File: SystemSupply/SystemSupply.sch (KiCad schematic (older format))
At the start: 14 parts

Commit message: Added DC/DC converters symbols to Library. Added DC/DC converters, purging valve parts and bus connectors to the SystemSupply schematic.
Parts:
- removed NT?: Net-Tie_2, symbol Device:Net-Tie_2
- added C?: 10n, symbol Device:C
- added C?: 470u, symbol Device:CP
- added C?: 180u, symbol Device:CP
- added D? (x2): D_ALT, symbol Device:D_ALT
- added D?: D_TVS_ALT, symbol Device:D_TVS_ALT
- added J? (x2): 4P4C, symbol Connector:4P4C
- added J? (x3): Screw_Terminal_01x02, symbol Connector:Screw_Terminal_01x02
- added JP?: Jumper_NO_Small, symbol Device:Jumper_NO_Small
- added L? (x2): 3u, symbol Device:L
- added Q?: Q_NMOS_GSD, symbol Device:Q_NMOS_GSD
- added R?: 1Meg, symbol Device:R
- added R?: 2k, symbol Device:R
- added R?: 10k, symbol Device:R
- added R?: 120, symbol Device:R
- added SW? (x2): SW_SPST, symbol Switch:SW_SPST
- added SW?: SW_Push, symbol Switch:SW_Push
- added U?: LTV-817S, Package_DIP:SMDIP-4_W9.53mm, symbol Isolator:LTV-817S
- added U?: DCDC_LM2596, symbol Library:DCDC_LM2596
- added U?: AXA01B18-L, symbol Library:AXA01B18-L
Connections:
- net labels added: +12V, IN+, IN-, OUT+, OUT-
- wire segments 20 -> 72
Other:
- note added: "Dodatkowe złącze magistrali"
- note added: "Filtr wejściowy"
- note added: "Filtr wyjściowy"
- note added: "Podły chińczyk"
- note added: "Przemysłowy pewniak"
- note added: "Przycisk zaworu wylotowego"
- note added: "Terminacja magistrali"
- note added: "Włącznik zasilania magistrali"
- note added: "Zasilanie sterownika ogniwa"
- note added: "Złącze elektrozaworu wylotowego"
- note added: "Złącze magistrali"
- note added: "Złącze sygnału elektrozaworu\nwylotowego"
- moved on the sheet: C?, D?, F?, J?, K?, Q?, R?, U?

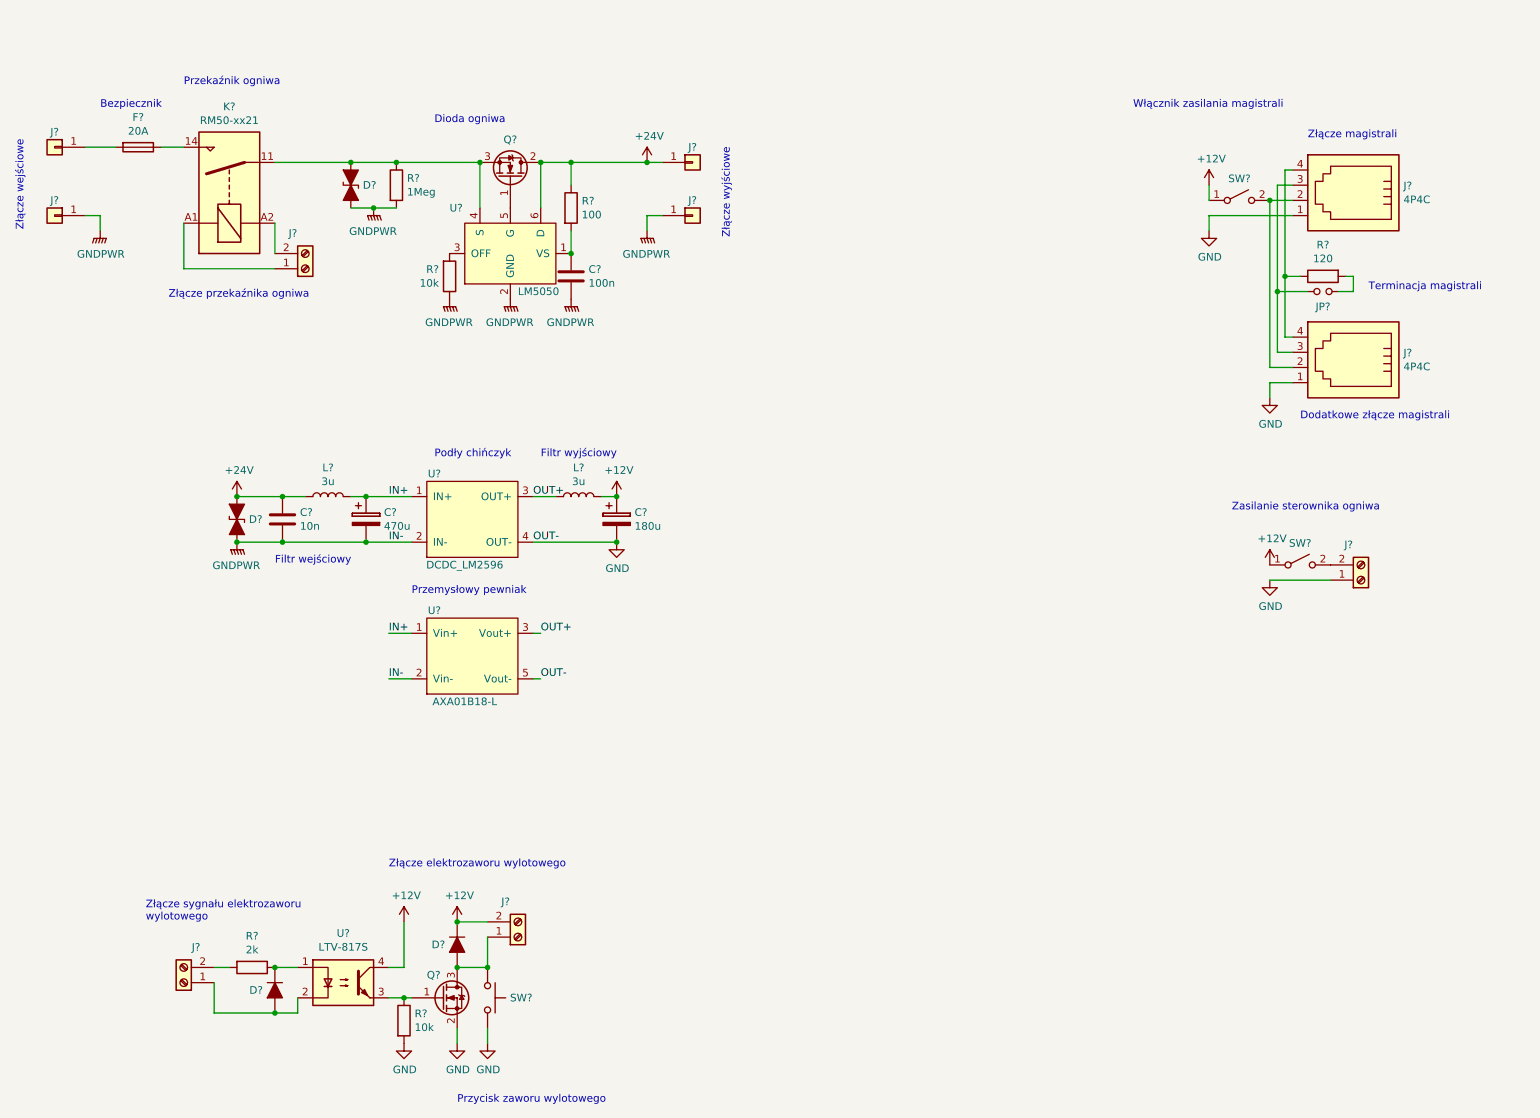
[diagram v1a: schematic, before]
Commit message: Added ground jumper.
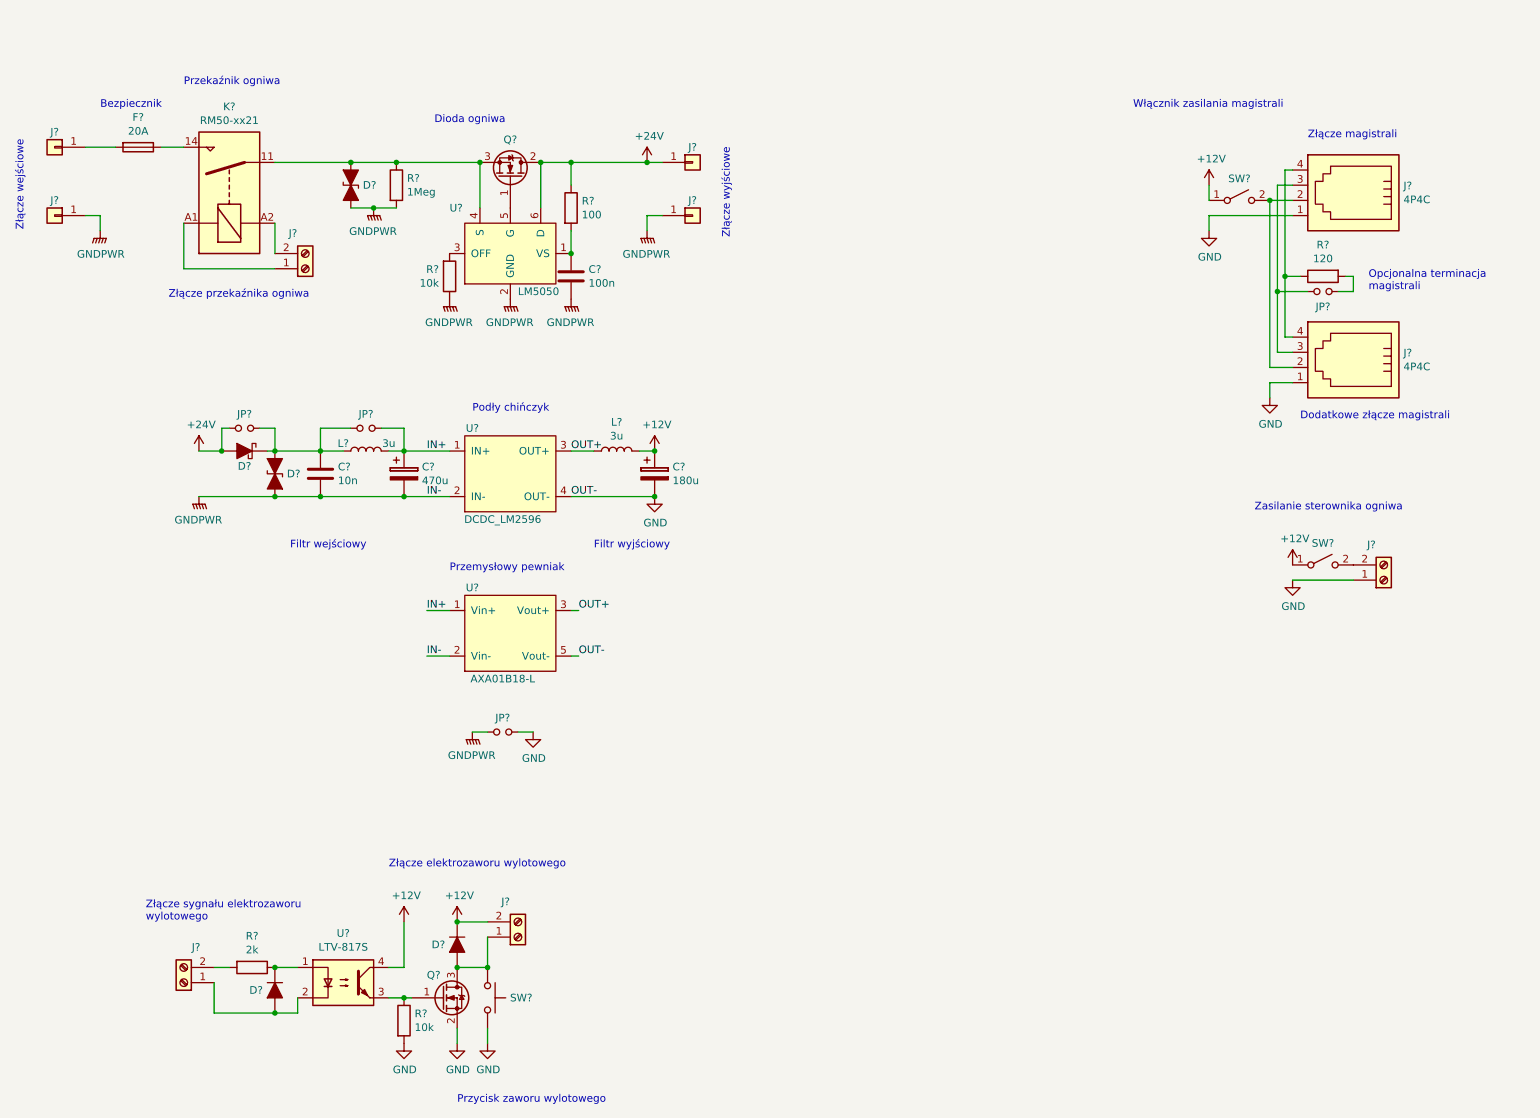
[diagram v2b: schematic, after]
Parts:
- added D?: D_Schottky_ALT, symbol Device:D_Schottky_ALT
- added JP? (x3): Jumper_NO_Small, symbol Device:Jumper_NO_Small
- C?: Type (none) -> X1
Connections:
- net +24V: now also D?.2 (A), JP?.1; no longer C?.1, D?.1 (A1), L?.1
- net GND: now also JP?.2
- net GNDPWR: now also JP?.1
- net IN+: now also JP?.2
- new net: C?.1, D?.1 (A1), D?.1 (K), JP?.1, JP?.2, L?.1
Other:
- note added: "Opcjonalna terminacja\nmagistrali"
- note removed: "Terminacja magistrali"
- moved on the sheet: C?, D?, J?, L?, SW?, U?

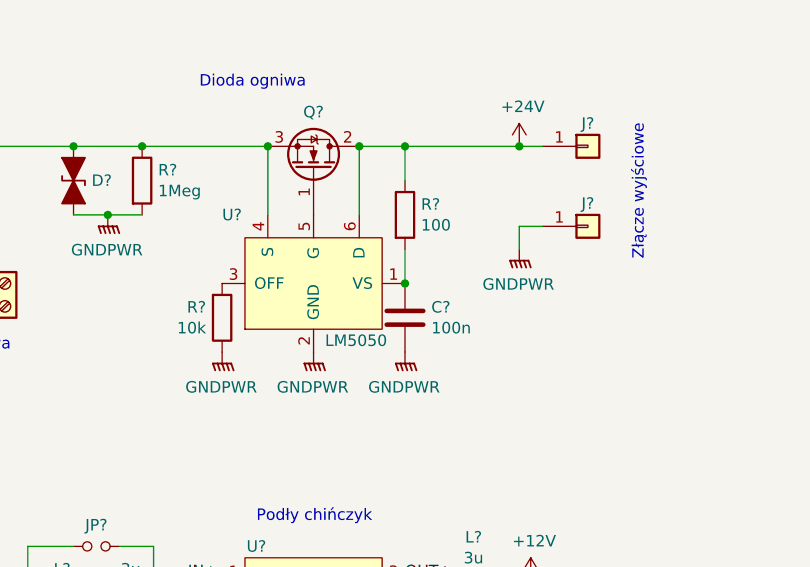
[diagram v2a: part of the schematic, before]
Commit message: Footprint feature. Added some footprints to library.
Squashed commit of the following:

commit cd975fe41aefde478091de7f14ed38d0983c180d
Author: Paweł <mackipawel@gmail.com>
Date:   Tue Mar 26 21:11:20 2019 +0100

    Added RFM18 and 5MS1S102AM2QE footprints.

commit 4e602ef25fbcf5dd6c485f40bf8f72e3bcba2156
Merge: 6566fa8 80250b1
Author: Asiderr <norkam41@gmail.com>
Date:   Thu Mar 21 22:21:42 2019 +0100

    merge

commit 6566fa87254b74c1a8c88ea40d35451463bde8d8
Author: Asiderr <norkam41@gmail.com>
Date:   Thu Mar 21 22:13:41 2019 +0100

    Adding footprints of RJ9, DC/DC converter

commit 80250b18490f042be3a2014c95d5388371debc3d
Author: Paweł <mackipawel@gmail.com>
Date:   Thu Mar 21 22:08:10 2019 +0100

    Removed backup files from git.

commit 04658cd3c50c023263e023466e96f3f94a65df95
Merge: 7849973 bad73f3
Author: Paweł <mackipawel@gmail.com>
Date:   Thu Mar 21 22:07:23 2019 +0100

    Merge branch 'feature/footprints' of https://github.com/EcoTechTeam/Hardware into feature/footprints

commit 78499733d111ae0bedf73c4fca8fcef50fc29226
Author: Paweł <mackipawel@gmail.com>
Date:   Thu Mar 21 22:07:10 2019 +0100

    Fixed footprint library name to Footprints.

commit 3f8eab394080d79e7aead60b2eec59a08122afbc
Author: Paweł <mackipawel@gmail.com>
Date:   Thu Mar 21 21:19:44 2019 +0100

    Removed tables.

commit 684012423bea3414343087823362922cefb8473a
Merge: b428dfb 1892ec1
Author: Paweł <mackipawel@gmail.com>
Date:   Thu Mar 21 21:19:12 2019 +0100

    Merge

commit bad73f3c705cb3c30d3a26163545b978ffddeb4c
Author: Asiderr <norkam41@gmail.com>
Date:   Thu Mar 21 00:16:46 2019 +0100

    Adding footprints of pasives, diodes, transistors

commit 1892ec1f2bc7f41887eec779a92ff03034286e97
Author: Asiderr <norkam41@gmail.com>
Date:   Wed Mar 20 23:04:53 2019 +0100

    Adding footprints to System Supply

commit b428dfbf710c4231b032b3b85412e614af8e604a
Author: Paweł <mackipawel@gmail.com>
Date:   Wed Mar 20 22:59:15 2019 +0100

    Added few footprints.

commit c791dd8f20d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
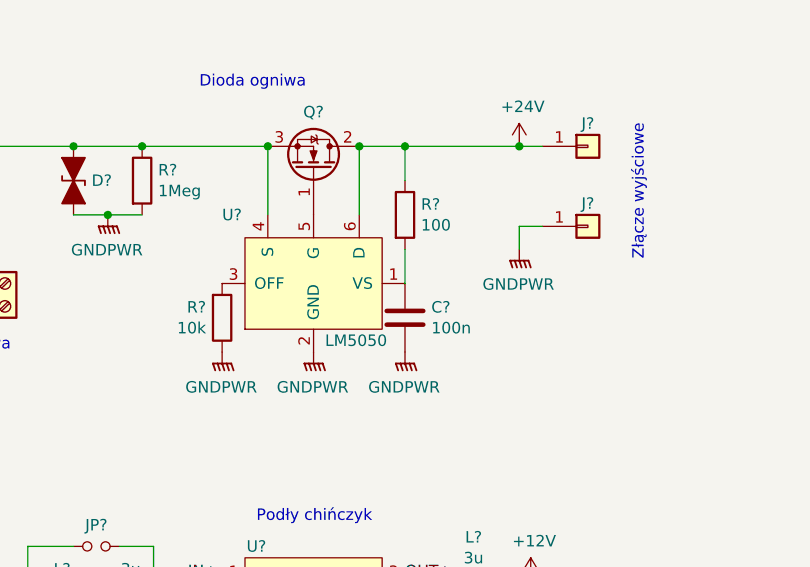
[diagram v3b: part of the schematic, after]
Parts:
- C? (x2): footprint (none) -> Capacitor_SMD:C_0603_1608Metric
- C? (x2): footprint (none) -> Capacitor_THT:C_Radial_D10.0mm_H20.0mm_P5.00mm
- D? (x2): footprint (none) -> Diode_SMD:D_SMC
- D? (x3): footprint (none) -> Diode_SMD:D_MiniMELF
- F?: footprint (none) -> Footprints:Fuse_Blade
- J? (x4): footprint (none) -> Footprints:TerminalBlock_DG250_02P
- J? (x2): footprint (none) -> Footprints:4P4C
- L?: footprint (none) -> Inductor_SMD:L_1812_4532Metric_Pad1.30x3.40mm_HandSolder
- L?: footprint (none) -> Inductor_SMD:L_1812_4532Metric
- Q? (x2): footprint (none) -> Package_TO_SOT_SMD:SOT-23
- R? (x6): footprint (none) -> Resistor_SMD:R_0603_1608Metric
- U?: footprint (none) -> Package_TO_SOT_SMD:SOT-23-6
- U?: footprint (none) -> Footprints:LM2596_Board
- U?: footprint (none) -> Footprints:AXA01B18-L
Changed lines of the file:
@@
 F 0 "F?" V 1303 1250 50  0000 C CNN
 F 1 "20A" V 1394 1250 50  0000 C CNN
-F 2 "" V 1430 1250 50  0001 C CNN
+F 2 "Footprints:Fuse_Blade" V 1430 1250 50  0001 C CNN
 F 3 "" H 1500 1250 50  0001 C CNN
 	1    1500 1250
@@
 F 0 "J?" H 2519 1817 50  0000 C CNN
 F 1 "Screw_Terminal_01x02" H 2520 1816 50  0001 C CNN
-F 2 "" H 2600 2050 50  0001 C CNN
+F 2 "Footprints:TerminalBlock_DG250_02P" H 2600 2050 50  0001 C CNN
 F 3 "" H 2600 2050 50  0001 C CNN
 	1    2600 2050
@@
 F 0 "Q?" V 4200 1450 50  0000 C CNN
 F 1 "Q_NMOS_GDS" V 4202 1450 50  0001 C CNN
-F 2 "" H 4150 1550 50  0001 C CNN
+F 2 "Package_TO_SOT_SMD:SOT-23" H 4150 1550 50  0001 C CNN
 F 3 "" H 3950 1450 50  0001 C CNN
 	1    3950 1450
@@
 F 0 "U?" H 3550 2250 50  0000 L CNN
 F 1 "LM5050" H 4000 1700 50  0000 L CNN
-F 2 "" H 3950 2200 50  0001 C CNN
+F 2 "Package_TO_SOT_SMD:SOT-23-6" H 3950 2200 50  0001 C CNN
 F 3 "" H 3950 2200 50  0001 C CNN
 	1    3950 1950
@@
 F 0 "R?" H 4420 1696 50  0000 L CNN
 F 1 "100" H 4420 1605 50  0000 L CNN
-F 2 "" V 4280 1650 50  0001 C CNN
+F 2 "Resistor_SMD:R_0603_1608Metric" V 4280 1650 50  0001 C CNN
 F 3 "" H 4350 1650 50  0001 C CNN
 	1    4350 1650
@@
 F 0 "C?" H 4465 2146 50  0000 L CNN
 F 1 "100n" H 4465 2055 50  0000 L CNN
-F 2 "" H 4388 1950 50  0001 C CNN
+F 2 "Capacitor_SMD:C_0603_1608Metric" H 4388 1950 50  0001 C CNN
 F 3 "" H 4350 2100 50  0001 C CNN
 	1    4350 2100
 	1    0    0    -1
 $EndComp
-Connection ~ 4350 1950
 $Comp
 L Device:R R?
@@
 F 0 "R?" H 3480 2054 50  0000 R CNN
 F 1 "10k" H 3480 2145 50  0000 R CNN
-F 2 "" V 3480 2100 50  0001 C CNN
+F 2 "Resistor_SMD:R_0603_1608Metric" V 3480 2100 50  0001 C CNN
 F 3 "" H 3550 2100 50  0001 C CNN
 	1    3550 2100
@@
 F 0 "D?" V 2900 1579 50  0000 L CNN
 F 1 "D_TVS_ALT" V 2945 1579 50  0001 L CNN
-F 2 "" H 2900 1500 50  0001 C CNN
+F 2 "Diode_SMD:D_SMC" H 2900 1500 50  0001 C CNN
 F 3 "" H 2900 1500 50  0001 C CNN
 	1    2900 1500
@@
 F 0 "J?" H 9170 1696 50  0000 R CNN
 F 1 "4P4C" H 9170 1605 50  0000 R CNN
-F 2 "" V 9500 1650 50  0001 C CNN
+F 2 "Footprints:4P4C" V 9500 1650 50  0001 C CNN
 F 3 "~" V 9500 1650 50  0001 C CNN
 	1    9500 1600
@@
 F 0 "J?" H 9170 2796 50  0000 R CNN
 F 1 "4P4C" H 9170 2705 50  0000 R CNN
-F 2 "" V 9500 2750 50  0001 C CNN
+F 2 "Footprints:4P4C" V 9500 2750 50  0001 C CNN
 F 3 "~" V 9500 2750 50  0001 C CNN
 	1    9500 2700
@@
 F 0 "R?" H 3270 1546 50  0000 L CNN
 F 1 "1Meg" H 3270 1455 50  0000 L CNN
-F 2 "" V 3130 1500 50  0001 C CNN
+F 2 "Resistor_SMD:R_0603_1608Metric" V 3130 1500 50  0001 C CNN
 F 3 "~" H 3200 1500 50  0001 C CNN
 	1    3200 1500
@@
 F 0 "J?" H 1719 6517 50  0000 C CNN
 F 1 "Screw_Terminal_01x02" H 1720 6516 50  0001 C CNN
-F 2 "" H 1800 6750 50  0001 C CNN
+F 2 "Footprints:TerminalBlock_DG250_02P" H 1800 6750 50  0001 C CNN
 F 3 "" H 1800 6750 50  0001 C CNN
 	1    1800 6750
@@
 F 0 "R?" V 2043 6650 50  0000 C CNN
 F 1 "2k" V 2134 6650 50  0000 C CNN
-F 2 "" V 2180 6650 50  0001 C CNN
+F 2 "Resistor_SMD:R_0603_1608Metric" V 2180 6650 50  0001 C CNN
 F 3 "~" H 2250 6650 50  0001 C CNN
 	1    2250 6650
@@
 F 0 "D?" V 2400 6879 50  0000 L CNN
 F 1 "D_ALT" V 2445 6879 50  0001 L CNN
-F 2 "" H 2400 6800 50  0001 C CNN
+F 2 "Diode_SMD:D_MiniMELF" H 2400 6800 50  0001 C CNN
 F 3 "~" H 2400 6800 50  0001 C CNN
 	1    2400 6800
@@
 F 0 "R?" H 3320 7046 50  0000 L CNN
 F 1 "10k" H 3320 6955 50  0000 L CNN
-F 2 "" V 3180 7000 50  0001 C CNN
+F 2 "Resistor_SMD:R_0603_1608Metric" V 3180 7000 50  0001 C CNN
 F 3 "~" H 3250 7000 50  0001 C CNN
 	1    3250 7000
@@
 F 0 "Q?" H 3400 7000 50  0000 L CNN
 F 1 "Q_NMOS_GSD" H 3705 6805 50  0001 L CNN
-F 2 "" H 3700 6950 50  0001 C CNN
+F 2 "Package_TO_SOT_SMD:SOT-23" H 3700 6950 50  0001 C CNN
 F 3 "~" H 3500 6850 50  0001 C CNN
 	1    3500 6850
@@
 F 0 "D?" V 3600 6579 50  0000 L CNN
 F 1 "D_ALT" V 3645 6579 50  0001 L CNN
-F 2 "" H 3600 6500 50  0001 C CNN
+F 2 "Diode_SMD:D_MiniMELF" H 3600 6500 50  0001 C CNN
 F 3 "~" H 3600 6500 50  0001 C CNN
 	1    3600 6500
@@
 F 0 "J?" H 3919 6217 50  0000 C CNN
 F 1 "Screw_Terminal_01x02" H 3920 6216 50  0001 C CNN
-F 2 "" H 4000 6450 50  0001 C CNN
+F 2 "Footprints:TerminalBlock_DG250_02P" H 4000 6450 50  0001 C CNN
 F 3 "" H 4000 6450 50  0001 C CNN
 	1    4000 6450
@@
 F 0 "R?" V 9093 2100 50  0000 C CNN
 F 1 "120" V 9184 2100 50  0000 C CNN
-F 2 "" V 9230 2100 50  0001 C CNN
+F 2 "Resistor_SMD:R_0603_1608Metric" V 9230 2100 50  0001 C CNN
 F 3 "~" H 9300 2100 50  0001 C CNN
 	1    9300 2100
@@
 F 0 "U?" H 3700 3700 50  0000 C CNN
 F 1 "DCDC_LM2596" H 3900 3100 50  0000 C CNN
-F 2 "" H 3800 3300 50  0001 C CNN
+F 2 "Footprints:LM2596_Board" H 3800 3300 50  0001 C CNN
 F 3 "" H 3800 3300 50  0001 C CNN
 	1    3950 3400
@@
 F 0 "D?" V 2400 3479 50  0000 L CNN
 F 1 "D_TVS_ALT" V 2445 3479 50  0001 L CNN
-F 2 "" H 2400 3400 50  0001 C CNN
+F 2 "Diode_SMD:D_SMC" H 2400 3400 50  0001 C CNN
 F 3 "" H 2400 3400 50  0001 C CNN
 	1    2400 3400
@@
 F 0 "C?" H 2815 3446 50  0000 L CNN
 F 1 "10n" H 2815 3355 50  0000 L CNN
-F 2 "" H 2738 3250 50  0001 C CNN
+F 2 "Capacitor_SMD:C_0603_1608Metric" H 2738 3250 50  0001 C CNN
 F 3 "~" H 2700 3400 50  0001 C CNN
 F 4 "X1" H 2700 3400 50  0001 C CNN "Type"
@@
 F 0 "C?" H 3368 3446 50  0000 L CNN
 F 1 "470u" H 3368 3355 50  0000 L CNN
-F 2 "" H 3288 3250 50  0001 C CNN
+F 2 "Capacitor_THT:C_Radial_D10.0mm_H20.0mm_P5.00mm" H 3288 3250 50  0001 C CNN
 F 3 "~" H 3250 3400 50  0001 C CNN
 F 4 "50V" H 3250 3400 50  0001 C CNN "Voltage"
@@
 F 0 "J?" H 9619 3867 50  0000 C CNN
 F 1 "Screw_Terminal_01x02" H 9620 3866 50  0001 C CNN
-F 2 "" H 9700 4100 50  0001 C CNN
+F 2 "Footprints:TerminalBlock_DG250_02P" H 9700 4100 50  0001 C CNN
 F 3 "" H 9700 4100 50  0001 C CNN
 	1    9700 4100
@@
 F 0 "C?" H 5018 3446 50  0000 L CNN
 F 1 "180u" H 5018 3355 50  0000 L CNN
-F 2 "" H 4938 3250 50  0001 C CNN
+F 2 "Capacitor_THT:C_Radial_D10.0mm_H20.0mm_P5.00mm" H 4938 3250 50  0001 C CNN
 F 3 "~" H 4900 3400 50  0001 C CNN
 F 4 "50V" H 4900 3400 50  0001 C CNN "Voltage"
@@
 F 0 "L?" V 4840 3250 50  0000 C CNN
 F 1 "3u" V 4749 3250 50  0000 C CNN
-F 2 "" H 4650 3250 50  0001 C CNN
+F 2 "Inductor_SMD:L_1812_4532Metric" H 4650 3250 50  0001 C CNN
 F 3 "~" H 4650 3250 50  0001 C CNN
 F 4 "2A" V 4650 3250 50  0001 C CNN "Current"
@@
 F 0 "L?" V 3050 3400 50  0000 C CNN
 F 1 "3u" V 3050 3100 50  0000 C CNN
-F 2 "" H 3000 3250 50  0001 C CNN
+F 2 "Inductor_SMD:L_1812_4532Metric_Pad1.30x3.40mm_HandSolder" H 3000 3250 50  0001 C CNN
 F 3 "~" H 3000 3250 50  0001 C CNN
 	1    3000 3250
@@
 F 0 "U?" H 3700 4750 50  0000 C CNN
 F 1 "AXA01B18-L" H 3900 4150 50  0000 C CNN
-F 2 "" H 3950 4500 50  0001 C CNN
+F 2 "Footprints:AXA01B18-L" H 3950 4500 50  0001 C CNN
 F 3 "https://www.artesyn.com/power/assets/axa20w_02jul2015_183fdc184d.pdf" H 3950 4500 50  0001 C CNN
 	1    3950 4450
@@
 F 0 "D?" H 2200 3150 50  0000 C CNN
 F 1 "D_Schottky_ALT" H 2200 3375 50  0001 C CNN
-F 2 "" H 2200 3250 50  0001 C CNN
+F 2 "Diode_SMD:D_MiniMELF" H 2200 3250 50  0001 C CNN
 F 3 "~" H 2200 3250 50  0001 C CNN
 	1    2200 3250

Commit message: SystemSupply footprints
Squashed commit of the following:

commit 0bd7b2a681f9369231f8e24b93032b76762d25f9
Author: Paweł <mackipawel@gmail.com>
Date:   Mon Apr 1 21:54:14 2019 +0200

    Added FlatConnector and R30N relay footprints. Added all footprints to symbols on SystemSupply.

commit c64b223a18f0db3b17481c9f3533a511e4c60f06
Author: Paweł <mackipawel@gmail.com>
Date:   Sun Mar 31 23:01:21 2019 +0200

    Added few footprints.
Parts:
- removed K?: RM50-xx21, Relay_THT:Relay_SPST_Finder_32.21-x300, symbol Relay:RM50-xx21
- removed SW? (x2): SW_SPST, symbol Switch:SW_SPST
- added D2, D5: D_TVS_ALT, Diode_SMD:D_SMC, symbol Device:D_TVS_ALT
- added K1: R30N, Footprints:R30N, symbol Library:R30N
- added SW1, SW2: SW_SPDT, Footprints:5MS1S102AM6QE, symbol Switch:SW_SPDT
- F1: renamed from F?; footprint Footprints:Fuse_Blade -> Footprints:Fuse_Blade_90
- J1, J2, J4, J5: renamed from J?; footprint (none) -> Footprints:FlatConnector_63
- JP1, JP2, JP3, JP4: renamed from JP?; footprint (none) -> Jumper:SolderJumper-2_P1.3mm_Open_TrianglePad1.0x1.5mm
- Q1: renamed from Q?; footprint Package_TO_SOT_SMD:SOT-23 -> Package_TO_SOT_SMD:TO-263-2
- R1: renamed from R?; footprint Resistor_SMD:R_0603_1608Metric -> Resistor_THT:R_Axial_DIN0204_L3.6mm_D1.6mm_P5.08mm_Horizontal
- SW3: renamed from SW?; footprint (none) -> Button_Switch_THT:SW_PUSH-12mm
- U4: renamed from U?; footprint Package_DIP:SMDIP-4_W9.53mm -> Package_DIP:DIP-4_W7.62mm_LongPads
- gave numbers to parts that had none: 26
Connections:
- wire segments 85 -> 97
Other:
- moved on the sheet: F1, J2, J6
